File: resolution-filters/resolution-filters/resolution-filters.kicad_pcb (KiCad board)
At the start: 2 copper layers, 91.7 x 48.8 mm, 52 parts, among them J501 Conn_Coaxial, J502 691137710002, J503 Conn_Coaxial, K501 G5V-1, K502 G5V-1, T501 Transformer_1P_1S, T502 Transformer_1P_1S, Y501 Crystal_GND3_Small, Y502 Crystal_GND3_Small, Y503 Crystal_GND3_Small, Y504 Crystal_GND3_Small

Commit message: resolution filter board layout
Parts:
- moved D502 3.64 mm to (177.8, 80.2)
- moved J502 3.35 mm to (187.5, 84.5)
- moved L504 3.12 mm to (167.5, 77.0)
- moved R508 3.06 mm to (181.3, 72.6)
- moved D501 2.87 mm to (164.5, 66.5)
- moved R504 2.42 mm to (175.1, 66.8)
- moved L502 2.19 mm to (130.6, 77.0)
- moved L503 2.08 mm to (149.0, 77.0)
- moved C515 2.06 mm to (139.5, 80.3)
- moved C520 2.04 mm to (157.9, 80.2)
- moved J501 1.55 mm to (104.5, 99.0)
- moved H503 1.36 mm to (187.5, 68.5)
- moved H502 1.29 mm to (106.5, 106.5)
- moved H504 1.13 mm to (187.5, 106.5)
- moved Y504 0.98 mm to (162.3, 105.3)
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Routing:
- net /501-in: track 0.00 -> 108.3 mm
- net Net-(C511-Pad1): track 0.00 -> 30.6 mm
- net Net-(C519-Pad2): track 0.00 -> 29.6 mm
- net Net-(C514-Pad2): track 0.00 -> 28.5 mm
- net Net-(C509-Pad2): track 0.00 -> 27.6 mm
- net Net-(C501-Pad1): track 0.00 -> 26.9 mm
- net /502-in: track 0.00 -> 26.5 mm
- net Net-(C513-Pad1): track 0.00 -> 23.9 mm
- net Net-(C516-Pad1): track 0.00 -> 23.8 mm
- net Net-(K501-Pad5): track 0.00 -> 23.1 mm
- net Net-(C508-Pad1): track 0.00 -> 20.3 mm
- net Net-(C518-Pad1): track 0.00 -> 20.2 mm
- net Net-(J503-Pad1): track 0.00 -> 19.3 mm
- net Net-(C503-Pad3): track 0.00 -> 18.7 mm
- net Net-(C505-Pad1): track 0.00 -> 18.4 mm
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- added copper zone on B.Cu, net GND
- added copper zone on F.Cu, net GND
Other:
- board text added: "+15"
- board text added: "Andy McCann KA3KAF Doug McCann KA3KAG"
- board text added: "In"
- board text added: "Out"
- board text added: "Spectrum Analyzer Resolution Filter Rev O"

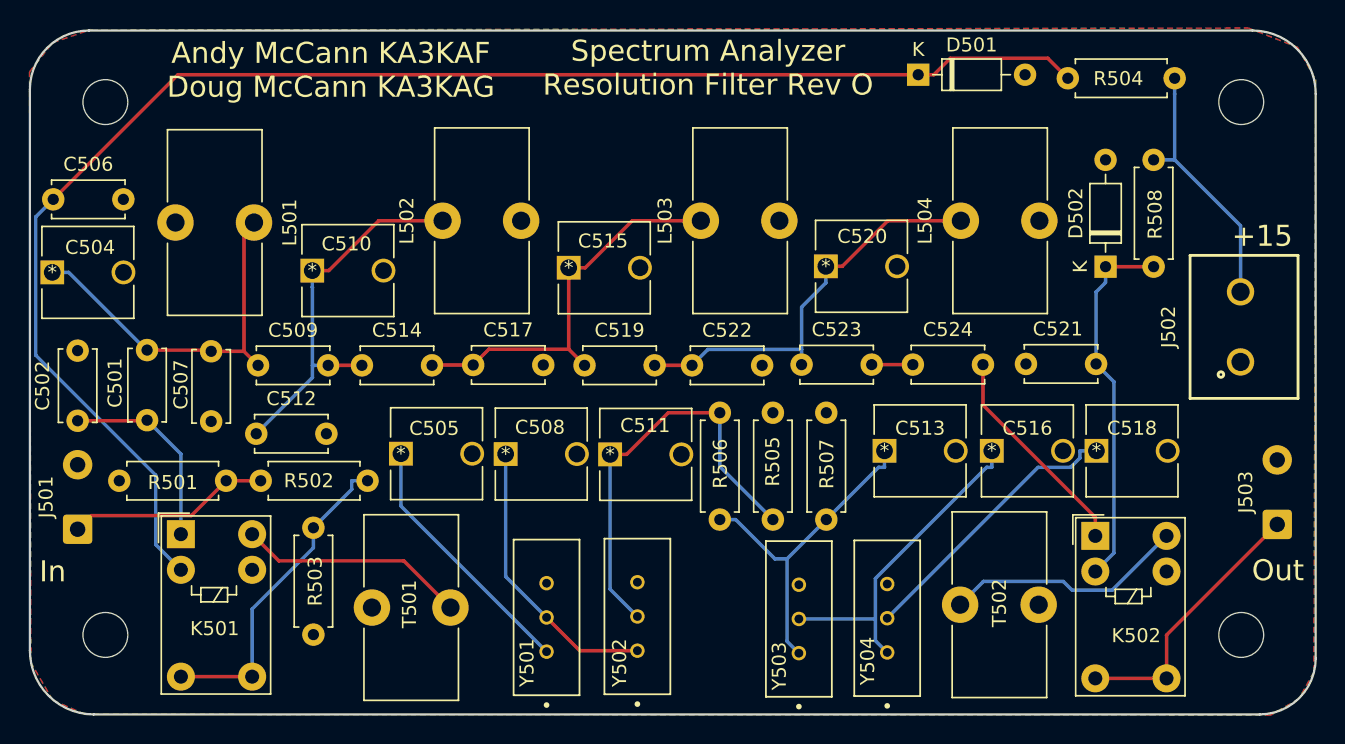
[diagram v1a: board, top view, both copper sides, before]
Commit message: updates to if log amp and resolution filter boards
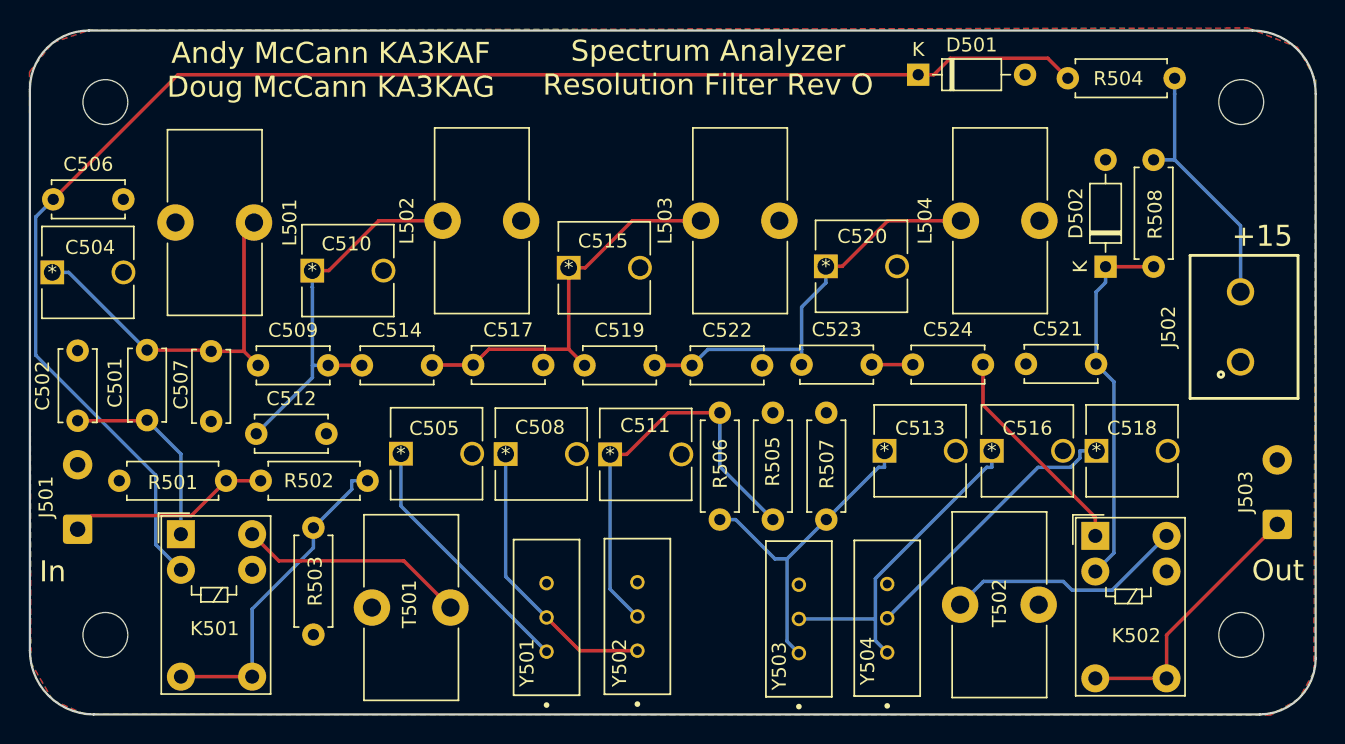
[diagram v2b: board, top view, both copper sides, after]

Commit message: fix transformer issue
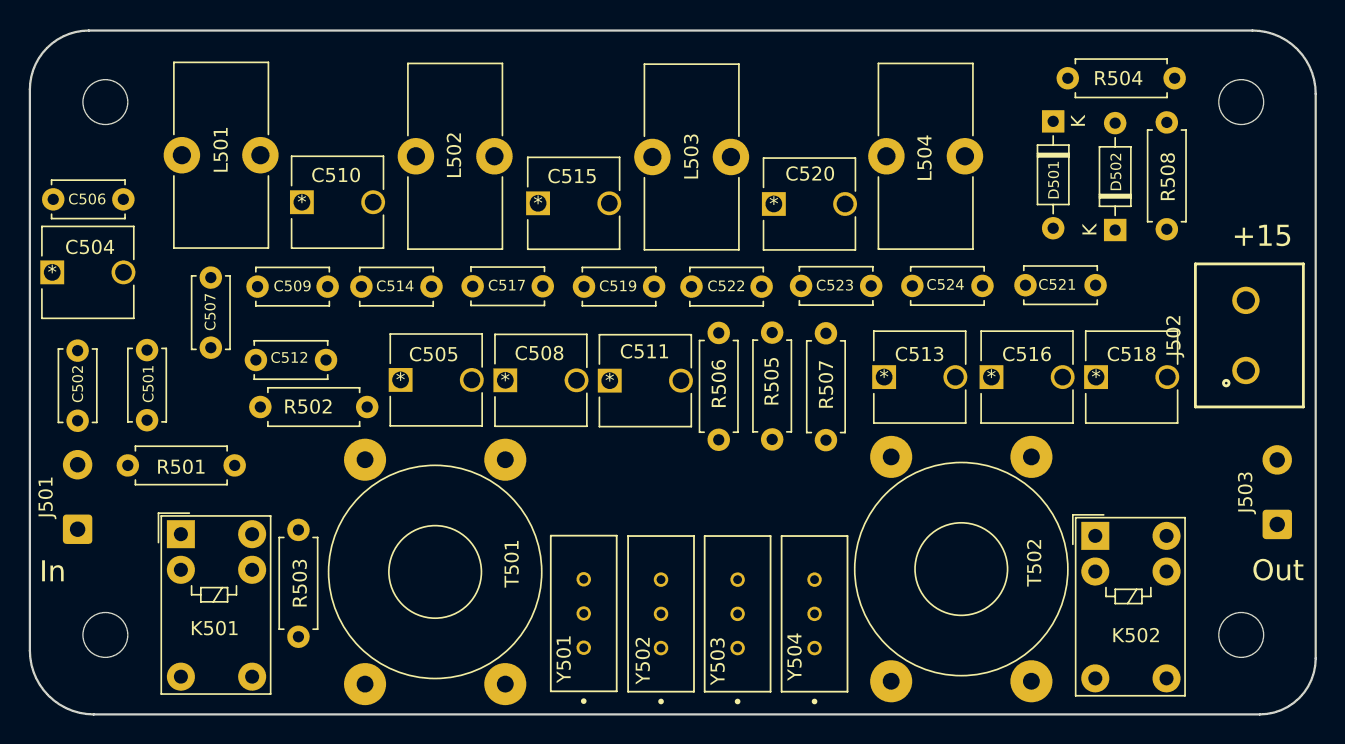
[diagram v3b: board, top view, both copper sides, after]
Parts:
- C504, C510, C515, C520: value 60p -> 12p-60p
- T501, T502: footprint Inductor_THT:L_Toroid_Vertical_L13.0mm_W6.5mm_P5.60mm -> Transformer_THT:Transformer_Toroid_Horizontal_D14.0mm_Amidon-T50
- Y501, Y502, Y503, Y504: value Crystal_GND3_Small -> 10.7MHz
- moved T501 12.2 mm to (125.0, 94.0)
- moved D501 10.2 mm to (174.1, 69.9), turned to -90 degrees
- moved T502 7.46 mm to (172.5, 109.8)
- moved L504 7.02 mm to (162.2, 72.4)
- moved C520 5.79 mm to (154.2, 75.8)
- moved R505 5.72 mm to (154.1, 92.6)
- moved L503 5.71 mm to (145.5, 72.4)
- moved R506 5.69 mm to (150.2, 85.0)
- moved R507 5.66 mm to (157.9, 92.6)
- moved C509 5.61 mm to (117.4, 81.7)
- moved C514 5.61 mm to (124.8, 81.7)
- moved C517 5.61 mm to (132.7, 81.6)
- moved C519 5.61 mm to (140.6, 81.7)
- moved C521 5.61 mm to (177.1, 81.6)
- moved C522 5.61 mm to (148.3, 81.7)
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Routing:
- net /501-in: track 108.3 -> 0.00 mm
- net Net-(C511-Pad1): track 30.6 -> 0.00 mm
- net Net-(C519-Pad2): track 29.6 -> 0.00 mm
- net Net-(C514-Pad2): track 28.5 -> 0.00 mm
- net Net-(C509-Pad2): track 27.6 -> 0.00 mm
- net Net-(C501-Pad1): track 26.9 -> 0.00 mm
- net /502-in: track 26.5 -> 0.00 mm
- net Net-(C513-Pad1): track 23.9 -> 0.00 mm
- net Net-(C516-Pad1): track 23.8 -> 0.00 mm
- net Net-(K501-Pad5): track 23.1 -> 0.00 mm
- net Net-(C508-Pad1): track 20.3 -> 0.00 mm
- net Net-(C518-Pad1): track 20.2 -> 0.00 mm
- net Net-(J503-Pad1): track 19.3 -> 0.00 mm
- net Net-(C503-Pad3): track 18.7 -> 0.00 mm
- net Net-(C505-Pad1): track 18.4 -> 0.00 mm
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- removed copper zone on B.Cu, net GND
- removed copper zone on F.Cu, net GND

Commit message: resolution filter improvement and bom
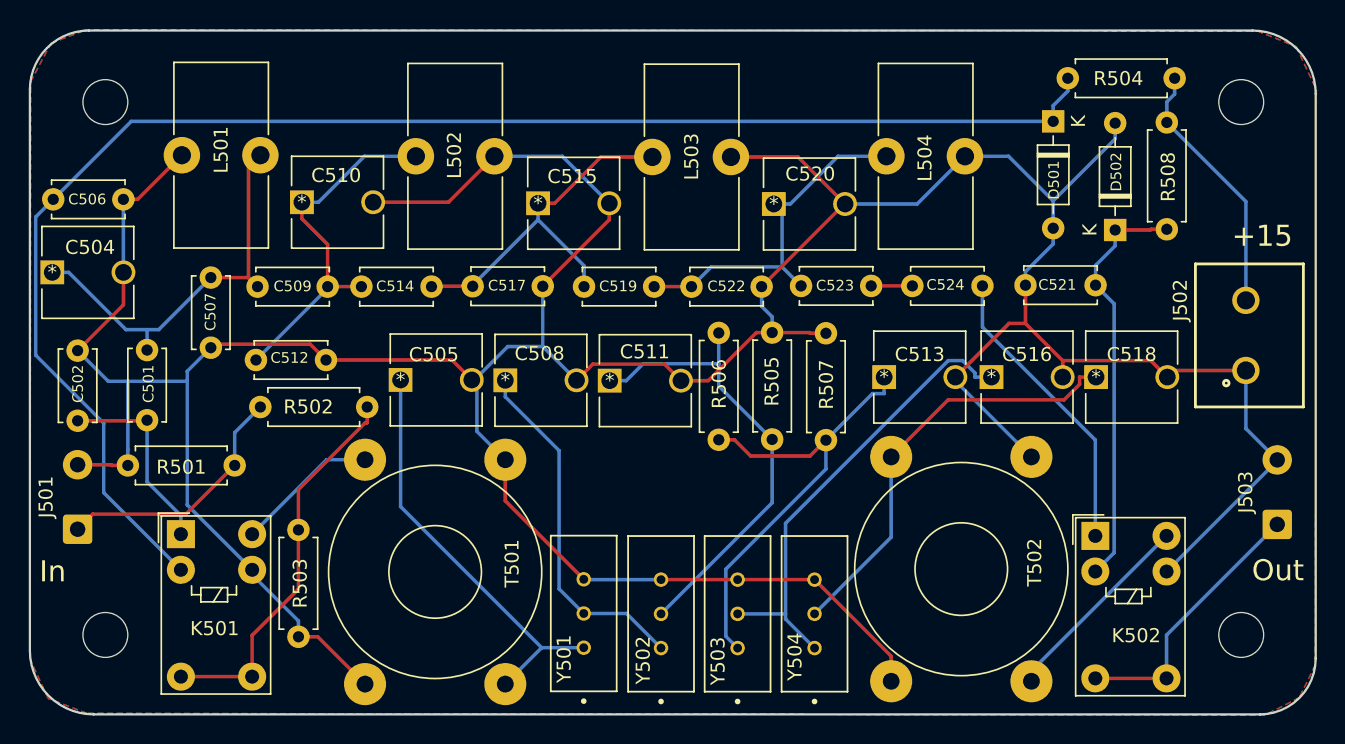
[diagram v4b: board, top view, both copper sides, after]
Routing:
- net GND: track 0.00 -> 299.1 mm
- net /501-in: track 0.00 -> 108.3 mm
- net Net-(C513-Pad1): track 0.00 -> 33.4 mm
- net Net-(C516-Pad1): track 0.00 -> 33.3 mm
- net Net-(C511-Pad1): track 0.00 -> 33.2 mm
- net Net-(C518-Pad1): track 0.00 -> 30.7 mm
- net Net-(C505-Pad1): track 0.00 -> 29.9 mm
- net /502-in: track 0.00 -> 29.7 mm
- net Net-(C501-Pad1): track 0.00 -> 28.7 mm
- net Net-(K501-Pad5): track 0.00 -> 27.8 mm
- net Net-(C514-Pad2): track 0.00 -> 26.4 mm
- net Net-(C509-Pad2): track 0.00 -> 26.0 mm
- net Net-(C519-Pad2): track 0.00 -> 25.5 mm
- net Net-(C508-Pad1): track 0.00 -> 25.5 mm
- net Net-(C524-Pad2): track 0.00 -> 21.2 mm
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- added copper zone on B.Cu, net GND
- added copper zone on F.Cu, net GND

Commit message: improved if and log amp and second lo/mixer
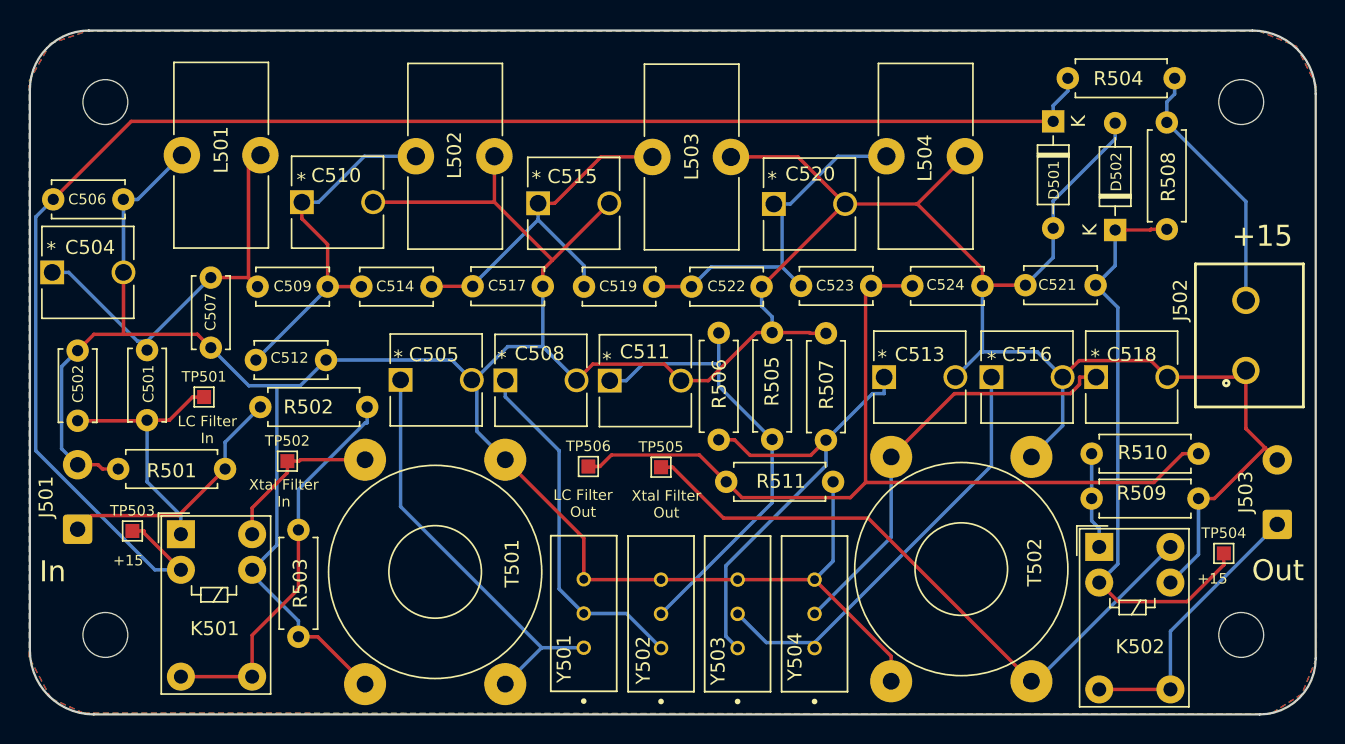
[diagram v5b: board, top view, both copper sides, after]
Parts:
- added R509: 10M, Resistor_THT:R_Axial_DIN0207_L6.3mm_D2.5mm_P7.62mm_Horizontal, F.Cu at (176.8, 96.8)
- added R510: 0, Resistor_THT:R_Axial_DIN0207_L6.3mm_D2.5mm_P7.62mm_Horizontal, F.Cu at (176.8, 93.6)
- added R511: 10M, Resistor_THT:R_Axial_DIN0207_L6.3mm_D2.5mm_P7.62mm_Horizontal, F.Cu at (150.8, 95.6)
- added TP501: TestPoint, TestPoint:TestPoint_Pad_1.0x1.0mm, F.Cu at (113.5, 89.5)
- added TP502: TestPoint, TestPoint:TestPoint_Pad_1.0x1.0mm, F.Cu at (119.5, 94.1)
- added TP503: TestPoint, TestPoint:TestPoint_Pad_1.0x1.0mm, F.Cu at (108.4, 99.1)
- added TP504: TestPoint, TestPoint:TestPoint_Pad_1.0x1.0mm, F.Cu at (186.3, 100.7)
- added TP505: TestPoint, TestPoint:TestPoint_Pad_1.0x1.0mm, F.Cu at (146.1, 94.5)
- added TP506: TestPoint, TestPoint:TestPoint_Pad_1.0x1.0mm, F.Cu at (140.9, 94.5)
- moved K502 0.84 mm to (177.4, 100.2)
- moved R501 0.73 mm to (115.0, 94.7)
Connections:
- C524 pad 2: Net-(C524-Pad2) -> GND
- K502 pad 1: Net-(C524-Pad2) -> Net-(K502-Pad1)
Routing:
- net Net-(C523-Pad2): track 2.94 -> 63.5 mm
- net Net-(K502-Pad10): track 14.4 -> 46.6 mm
- net Net-(C524-Pad2): track 21.2 -> 0.00 mm
- net /502-in: track 29.7 -> 42.0 mm
- net GND: track 299.1 -> 306.8 mm
- net Net-(K502-Pad1): track 0.00 -> 6.87 mm
- net /501-in: track 108.3 -> 114.1 mm
- net Net-(C501-Pad2): track 14.1 -> 18.8 mm
- net Net-(C516-Pad1): track 33.3 -> 30.9 mm
- net Net-(K501-Pad10): track 10.3 -> 11.8 mm
- net Net-(J503-Pad1): track 19.3 -> 20.0 mm
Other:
- board text added: "LC Filter In"
- board text added: "LC Filter Out"
- board text added: "Xtal Filter In"
- board text added: "Xtal Filter Out"

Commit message: resolution-filters update
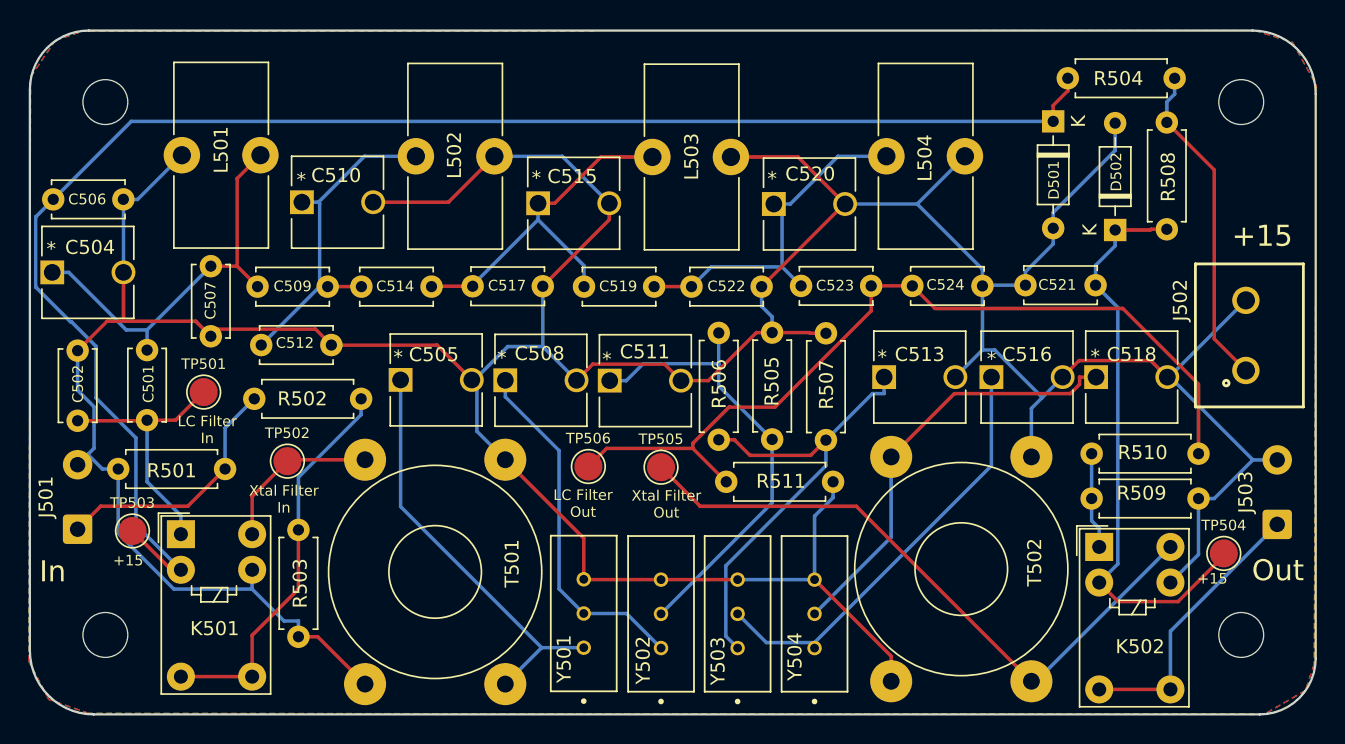
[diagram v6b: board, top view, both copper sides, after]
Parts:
- TP501, TP502, TP503, TP504, TP505, TP506: footprint TestPoint:TestPoint_Pad_1.0x1.0mm -> TestPoint:TestPoint_Pad_D2.0mm
- moved C512 1.13 mm to (117.6, 85.8)
- moved C507 0.81 mm to (114.0, 80.2)
- moved R502 0.73 mm to (117.1, 89.7)
- moved TP501 0.36 mm to (113.5, 89.2)
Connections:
- J502 pad 1: GND -> Net-(C503-Pad3)
- J502 pad 2: Net-(C503-Pad3) -> GND
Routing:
- net GND: track 306.8 -> 312.5 mm
- net Net-(C503-Pad3): track 18.4 -> 23.4 mm
- net Net-(C523-Pad2): track 63.5 -> 61.3 mm
- net Net-(C509-Pad2): track 26.0 -> 24.4 mm
- net /501-in: track 114.1 -> 113.0 mm

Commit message: Fix POS200 footprint and Terminal Block footprint of VCO 1st Mixer Board.  Rev 1.
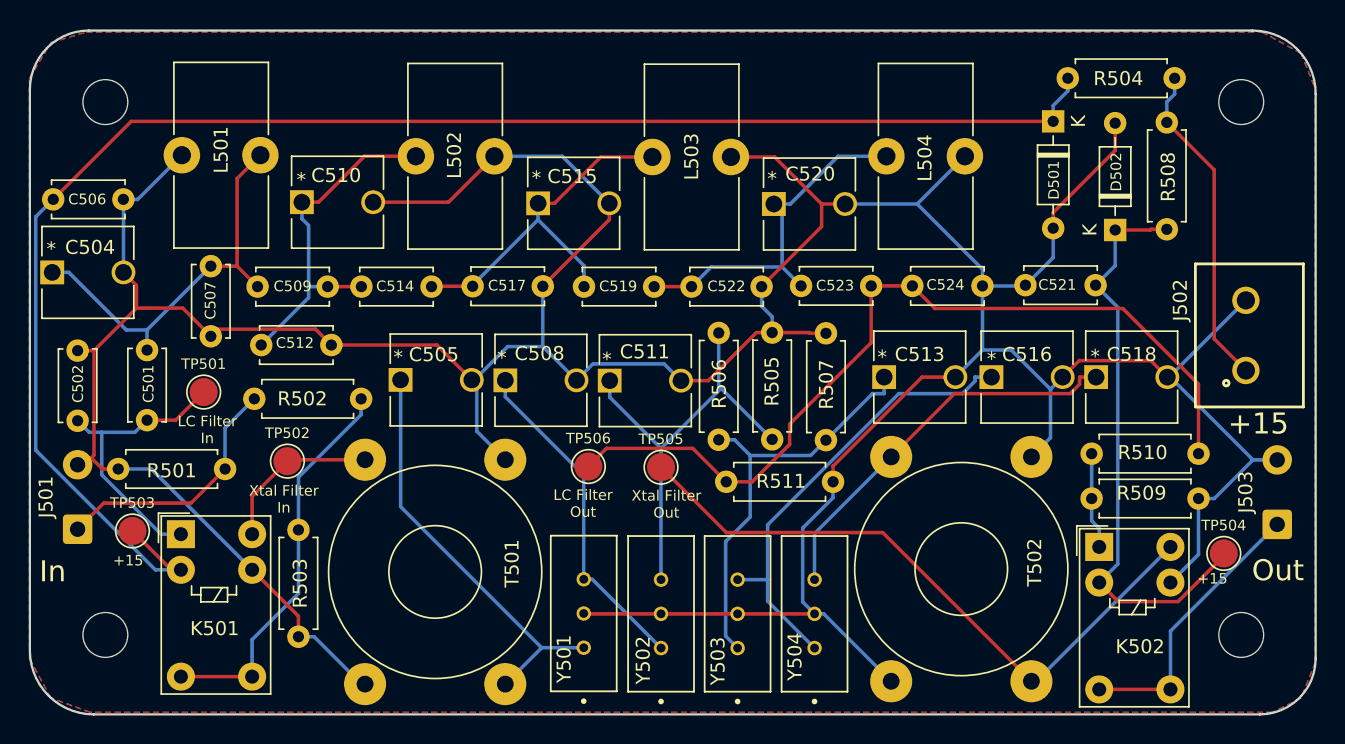
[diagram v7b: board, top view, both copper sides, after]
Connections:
- Y501 pad 2: Net-(C508-Pad1) -> GND
- Y501 pad 3: GND -> Net-(C508-Pad1)
- Y502 pad 2: Net-(C511-Pad1) -> GND
- Y502 pad 3: GND -> Net-(C511-Pad1)
- Y503 pad 2: Net-(C516-Pad1) -> GND
- Y503 pad 3: GND -> Net-(C516-Pad1)
- Y504 pad 2: Net-(C518-Pad1) -> GND
- Y504 pad 3: GND -> Net-(C518-Pad1)
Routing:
- net Net-(C513-Pad1): track 33.4 -> 30.1 mm
- net Net-(C518-Pad1): track 30.7 -> 28.3 mm
- net Net-(C511-Pad1): track 33.2 -> 30.9 mm
- net Net-(C501-Pad2): track 19.0 -> 21.0 mm
- net Net-(C516-Pad1): track 30.9 -> 32.8 mm
- net GND: track 312.5 -> 310.6 mm
- net Net-(C508-Pad1): track 25.5 -> 24.1 mm
- net /501-in: track 113.0 -> 114.0 mm
- net Net-(C509-Pad2): track 24.4 -> 25.0 mm
- net Net-(C523-Pad2): track 61.3 -> 61.9 mm
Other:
- board text added: "Spectrum Analyzer Resolution Filter Rev 1"
- board text removed: "Spectrum Analyzer Resolution Filter Rev O"
